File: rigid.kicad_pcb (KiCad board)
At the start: 4 copper layers, 33 x 35 mm, 58 parts, among them J1 47219-2001, J2 Bus_PCI_Express_Mini, J3 Battery, J4 USB_C_Receptacle_USB2.0, J5 FH34SRJ-6S-0.5SH(50), J6 FH34SRJ-6S-0.5SH(50), J7 Conn_01x02_Female, U1 STM32L432KCUx, U2 BQ24072RGTT, U3 TPS63020DSJR, U4 AW9523BTQR, U5 ALC5672

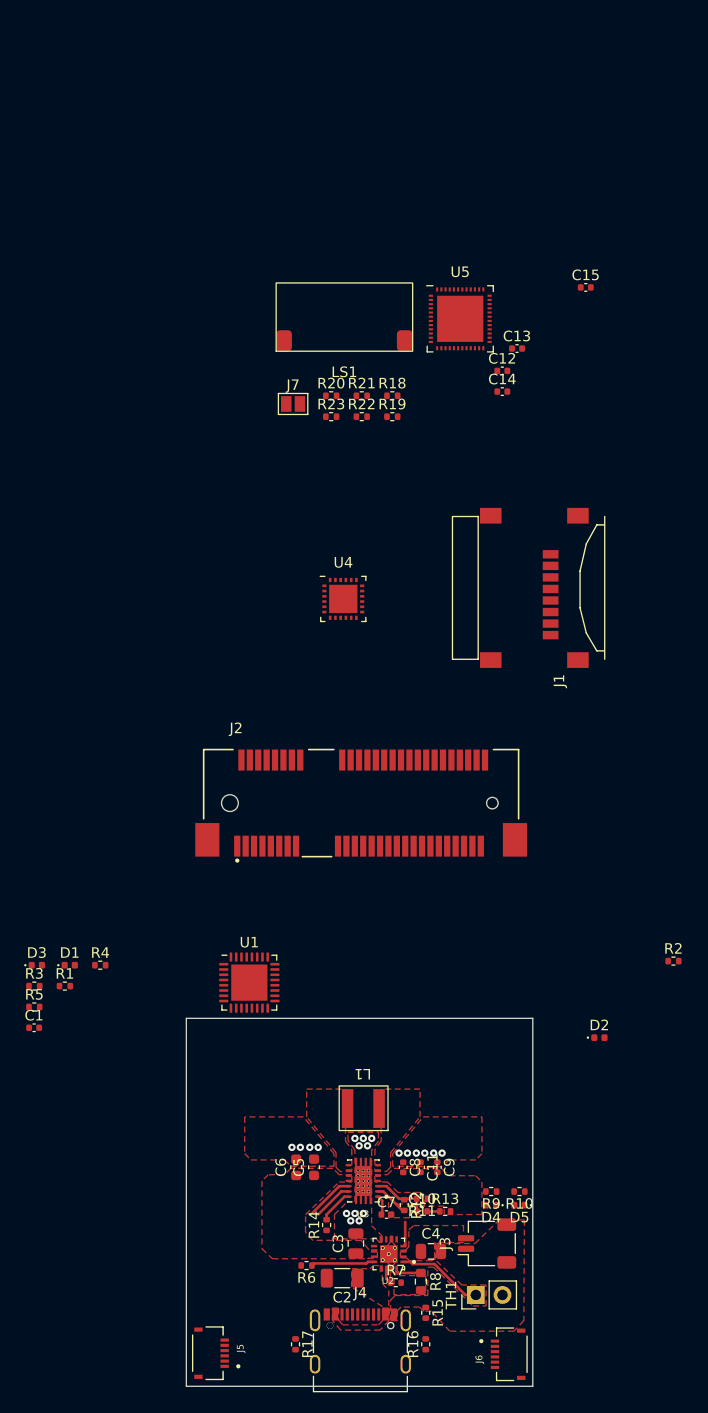
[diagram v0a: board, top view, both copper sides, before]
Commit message: Audio near completion
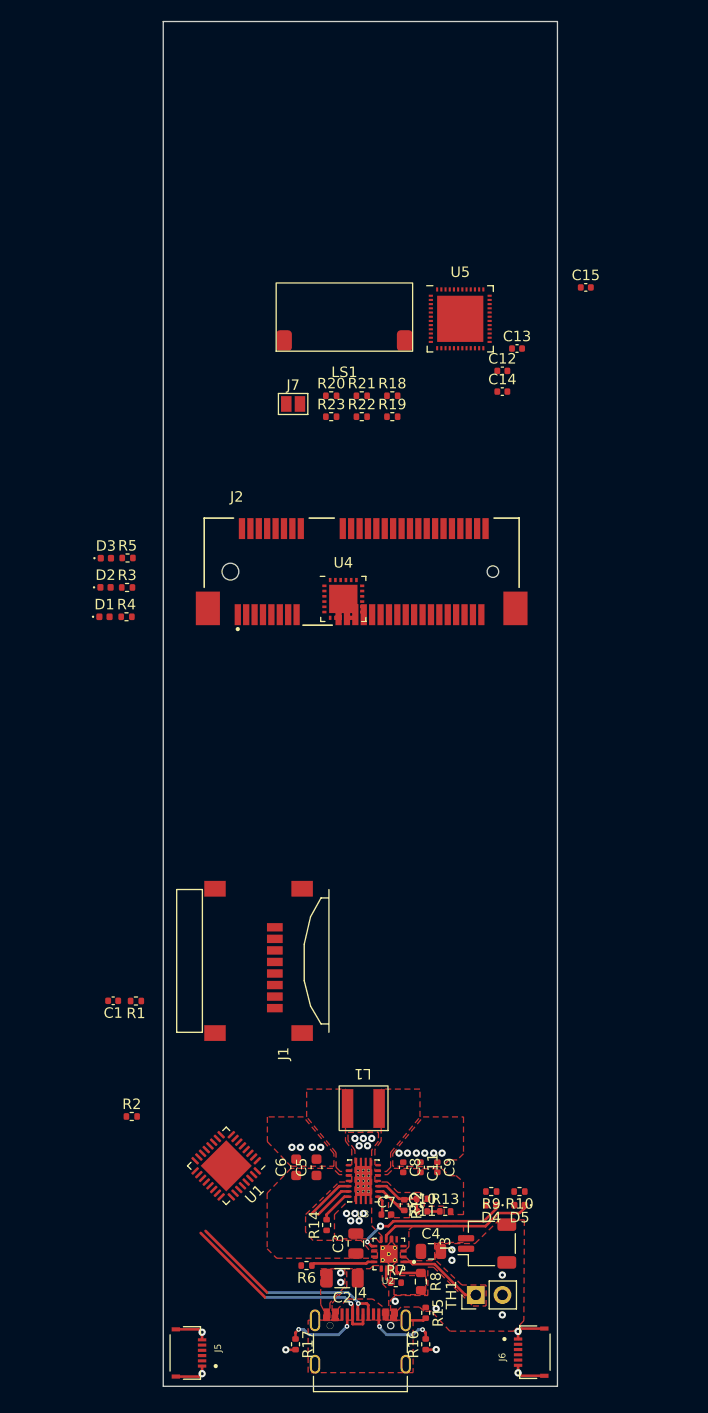
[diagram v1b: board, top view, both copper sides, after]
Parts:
- moved D2 63.7 mm to (101.3, 74.9)
- moved R2 53.7 mm to (103.8, 125.3)
- moved J1 44.2 mm to (115.3, 110.5)
- moved R5 43.7 mm to (103.4, 72.1)
- moved D3 39.3 mm to (101.3, 72.1)
- moved R3 39.0 mm to (103.4, 74.9)
- moved D1 33.4 mm to (101.2, 77.7)
- moved R4 33.3 mm to (103.3, 77.7)
- moved J2 22.1 mm to (123.9, 73.4)
- moved U1 17.6 mm to (112.8, 130.0), turned to -135 degrees
- moved C1 7.96 mm to (102.0, 114.3), turned to 180 degrees
- moved R1 6.92 mm to (104.2, 114.3), turned to 180 degrees
- moved J6 2.21 mm to (141.8, 147.8)
- moved J5 2.15 mm to (109.2, 147.8)
- moved C5 0.24 mm to (121.4, 130.1)
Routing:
- net USB_D-: track 0.00 -> 21.0 mm, vias 0 -> 1
- net USB_D+: track 0.00 -> 20.5 mm, vias 0 -> 1
- net GND: track 3.25 -> 18.5 mm, vias 0 -> 6
- net /Power/PG_BATT: track 0.00 -> 14.9 mm
- net /Power/CHG: track 0.00 -> 14.9 mm, vias 0 -> 2
- net Net-(J4-PadA5): track 0.00 -> 7.23 mm, vias 0 -> 2
- net Net-(J4-PadB5): track 0.00 -> 6.88 mm, vias 0 -> 2
- net /Power/CE: track 2.37 -> 0.00 mm
- net Net-(J4-PadS1): track 0.00 -> 1.99 mm
- net GNDPWR: vias 20 -> 28
- added copper zone on In2.Cu, net GND
- added copper zone on In2.Cu, net GNDPWR
- added copper zone on F.Cu, net Net-(J4-PadS1)
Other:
- board size 33 x 35 mm -> 37.5 x 130 mm
